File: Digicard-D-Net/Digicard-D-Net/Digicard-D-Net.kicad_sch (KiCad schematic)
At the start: 16 parts, among them IC1 74LS74, IC10 2764, IC11 74LS245, IC2 74LS00, IC3 74LS21, IC4 Z8530, IC6 74LS74, IC7 74LS00, IC8 74LS04, IC9 6264, P1 AppleIIBus, X1 3.6864 MHz

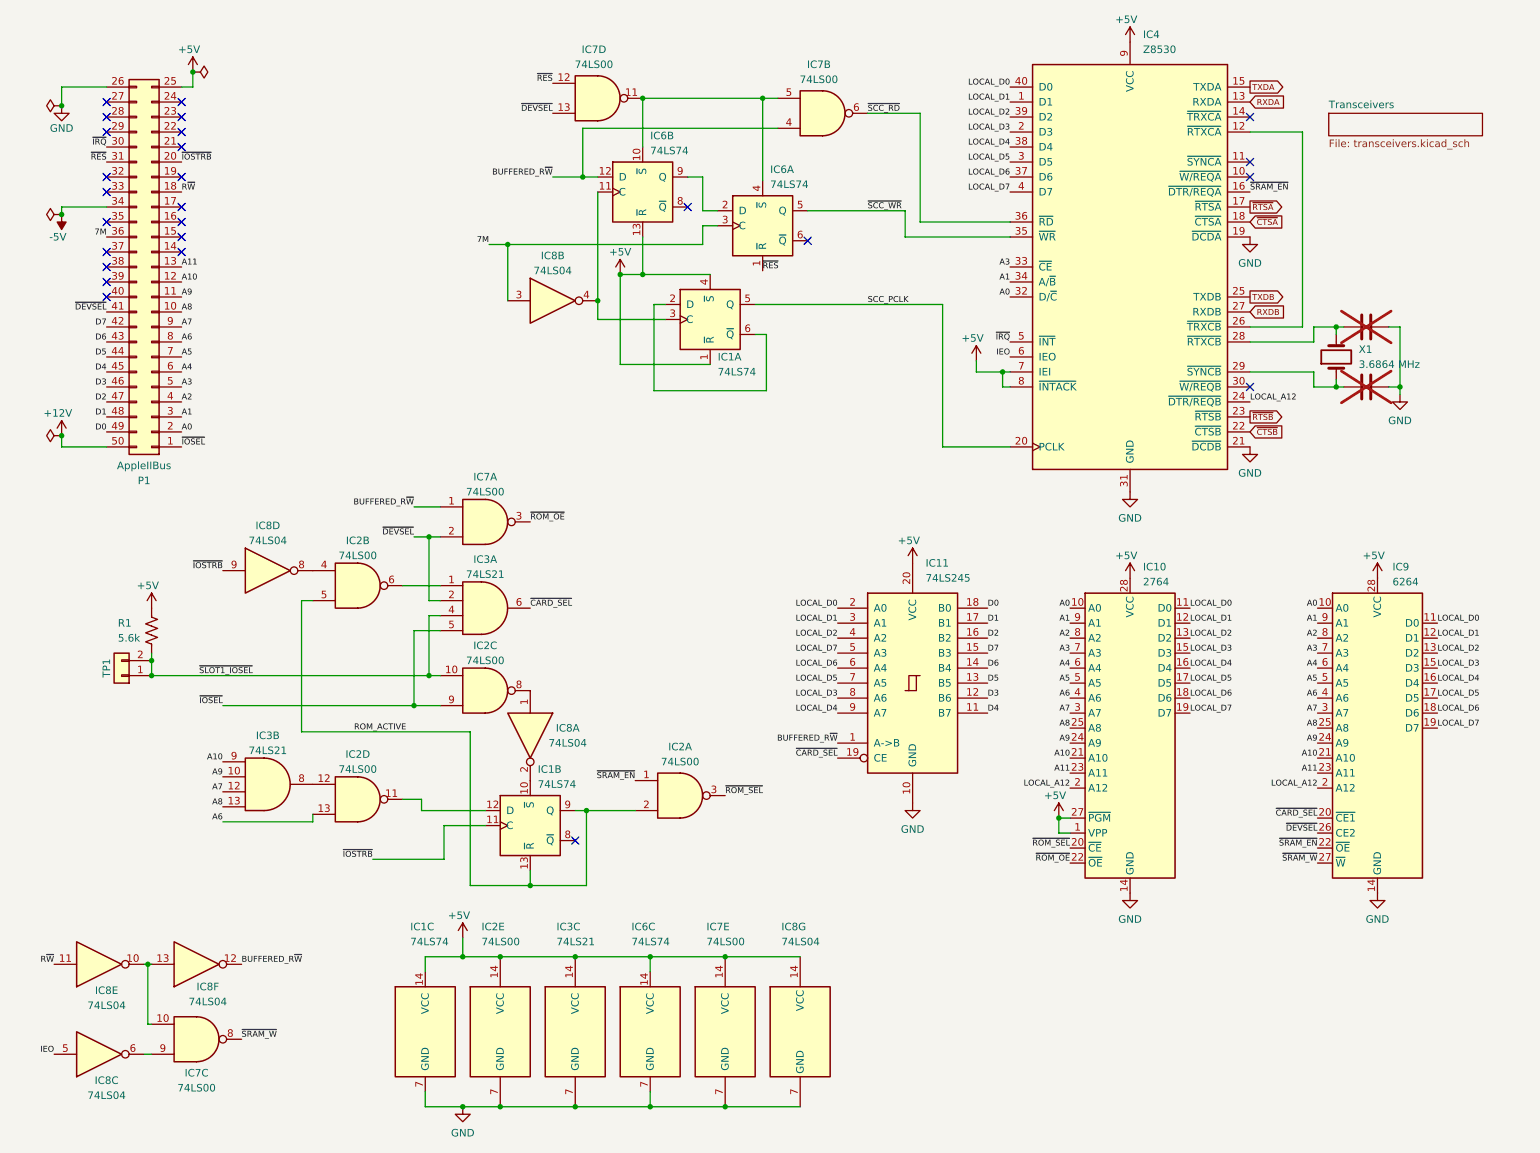
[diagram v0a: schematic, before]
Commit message: Update the Digicard projects to kicad8 and use the shared symbol library
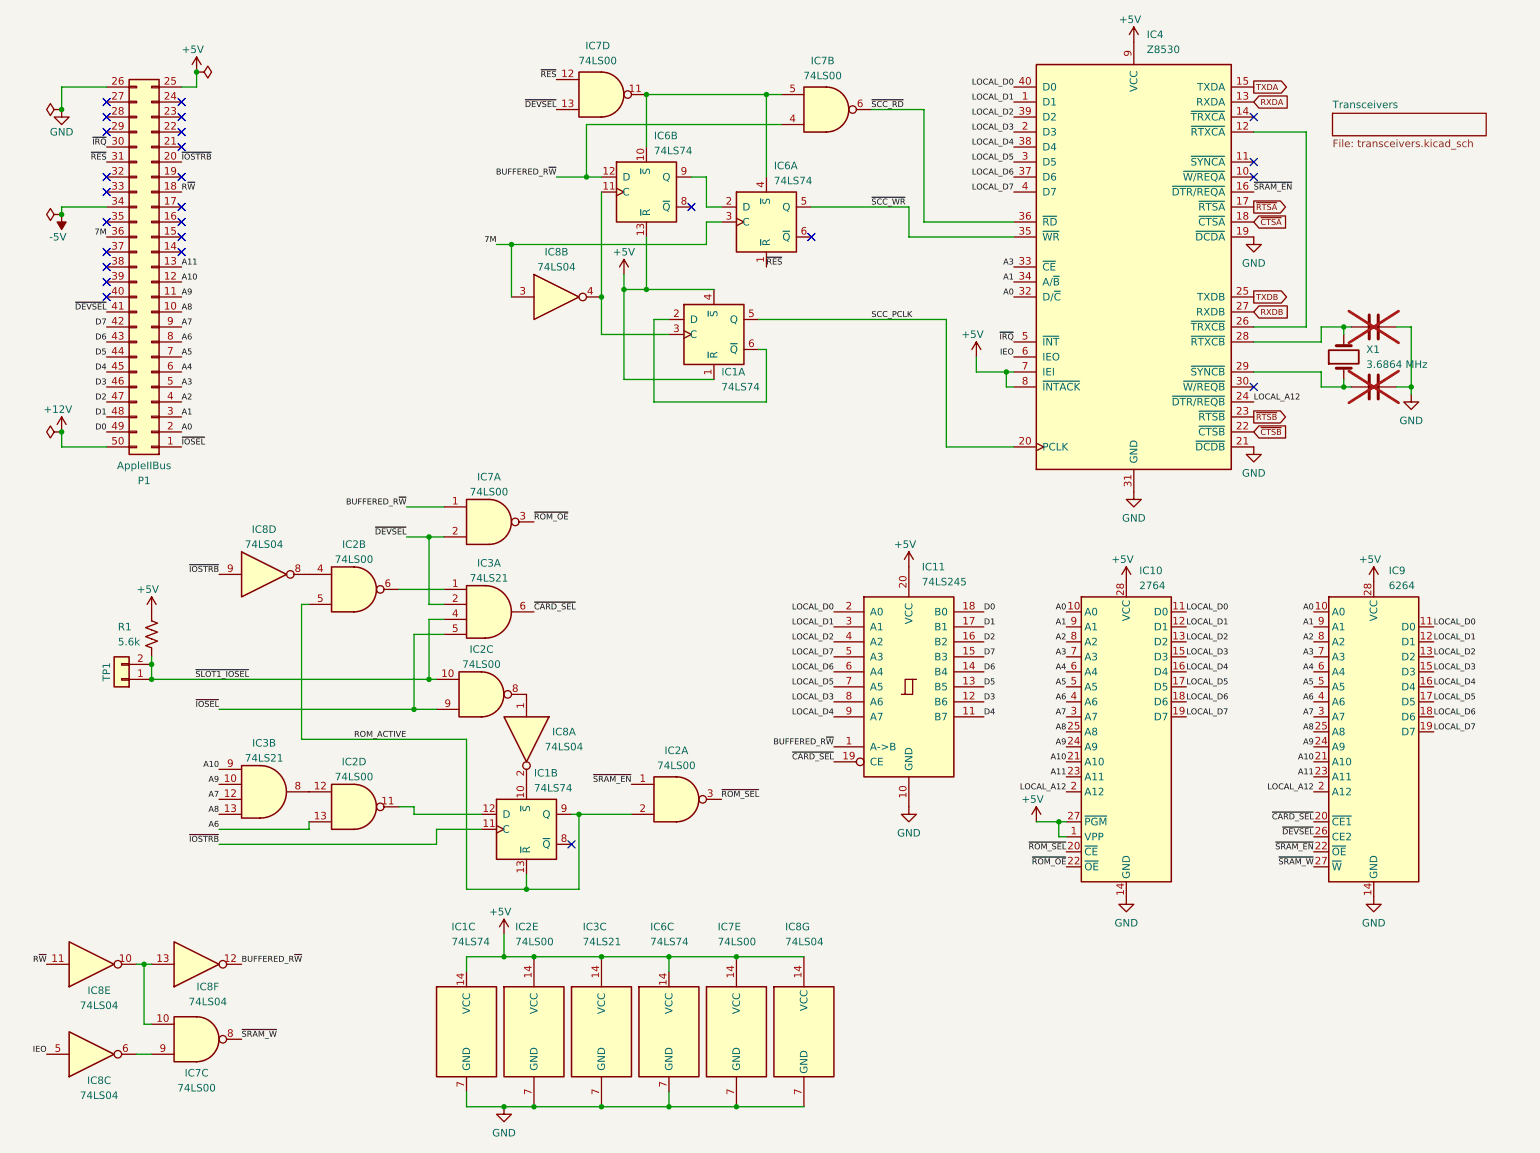
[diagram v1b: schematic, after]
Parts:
- IC9: symbol Memory:6264 -> Memory_Legacy:6264
- P1: footprint Apple:AppleIIBus_Edge -> (none)
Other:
- moved on the sheet: IC10, IC11, IC1A, IC1B, IC1C, IC2A, IC2B, IC2C, IC2D, IC2E, IC3A, IC3B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
